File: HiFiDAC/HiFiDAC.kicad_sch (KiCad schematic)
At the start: 48 parts, among them J1 SE, J2 I2S, J3 LDIFF, J4 RDIFF, J5 CTRL, J6 5V, J7 +-15V, U1 PCM1794A

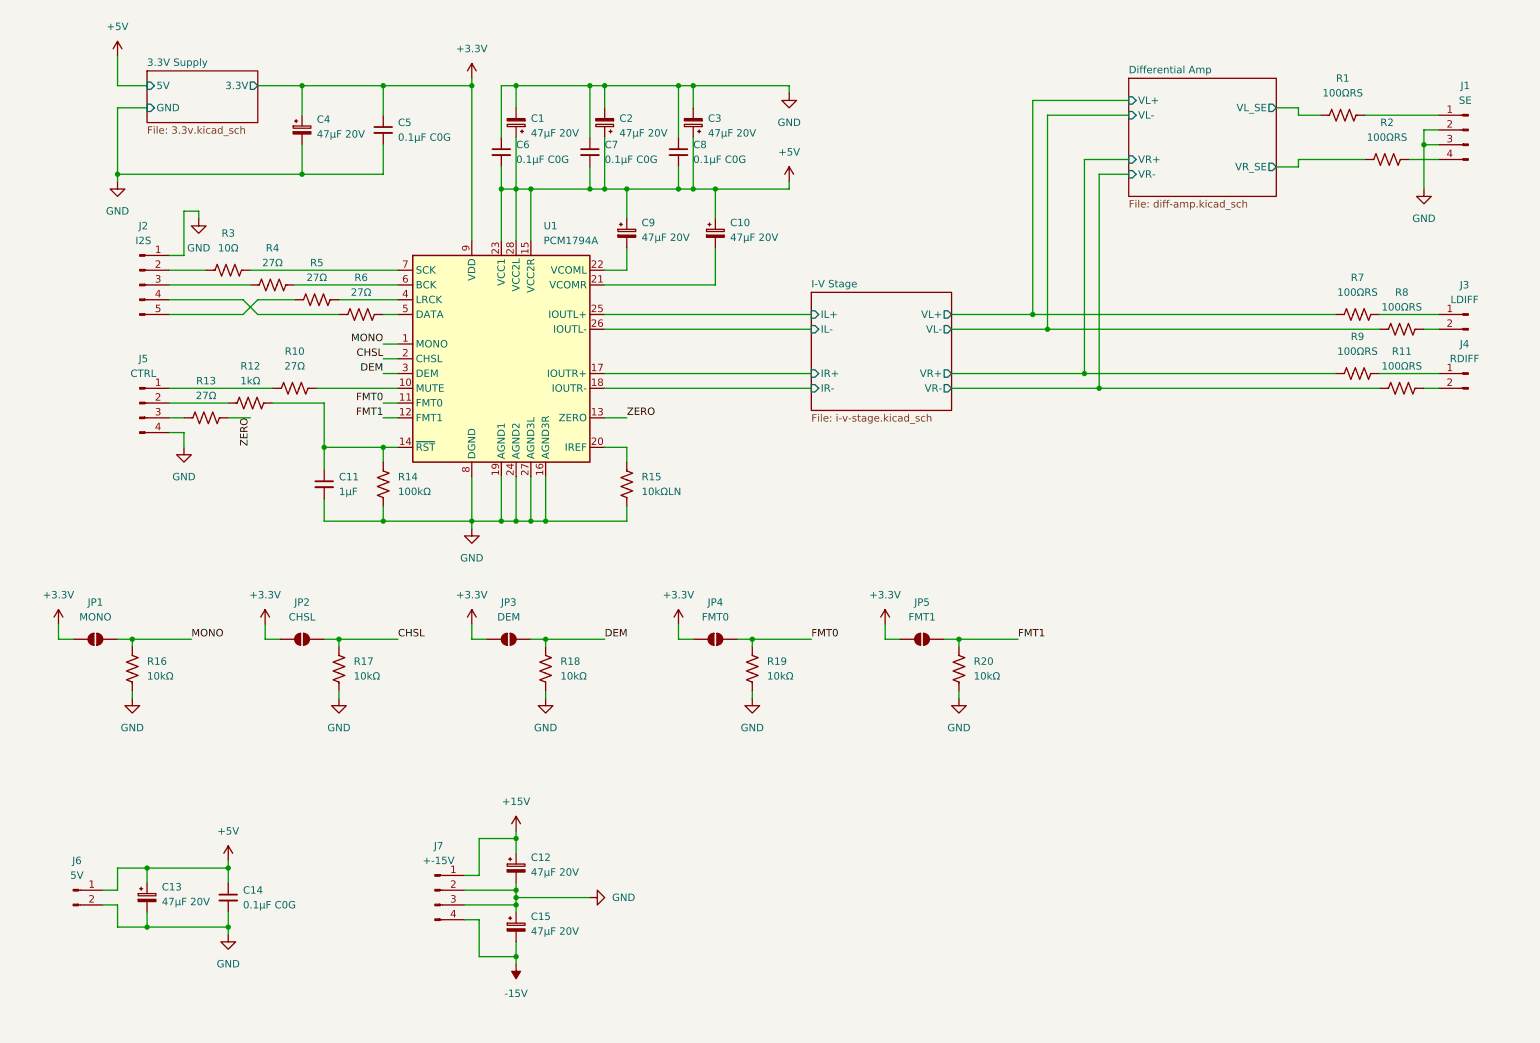
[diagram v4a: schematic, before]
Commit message: HiFiDAC redesign of clocking, digital IO, ferrite beads
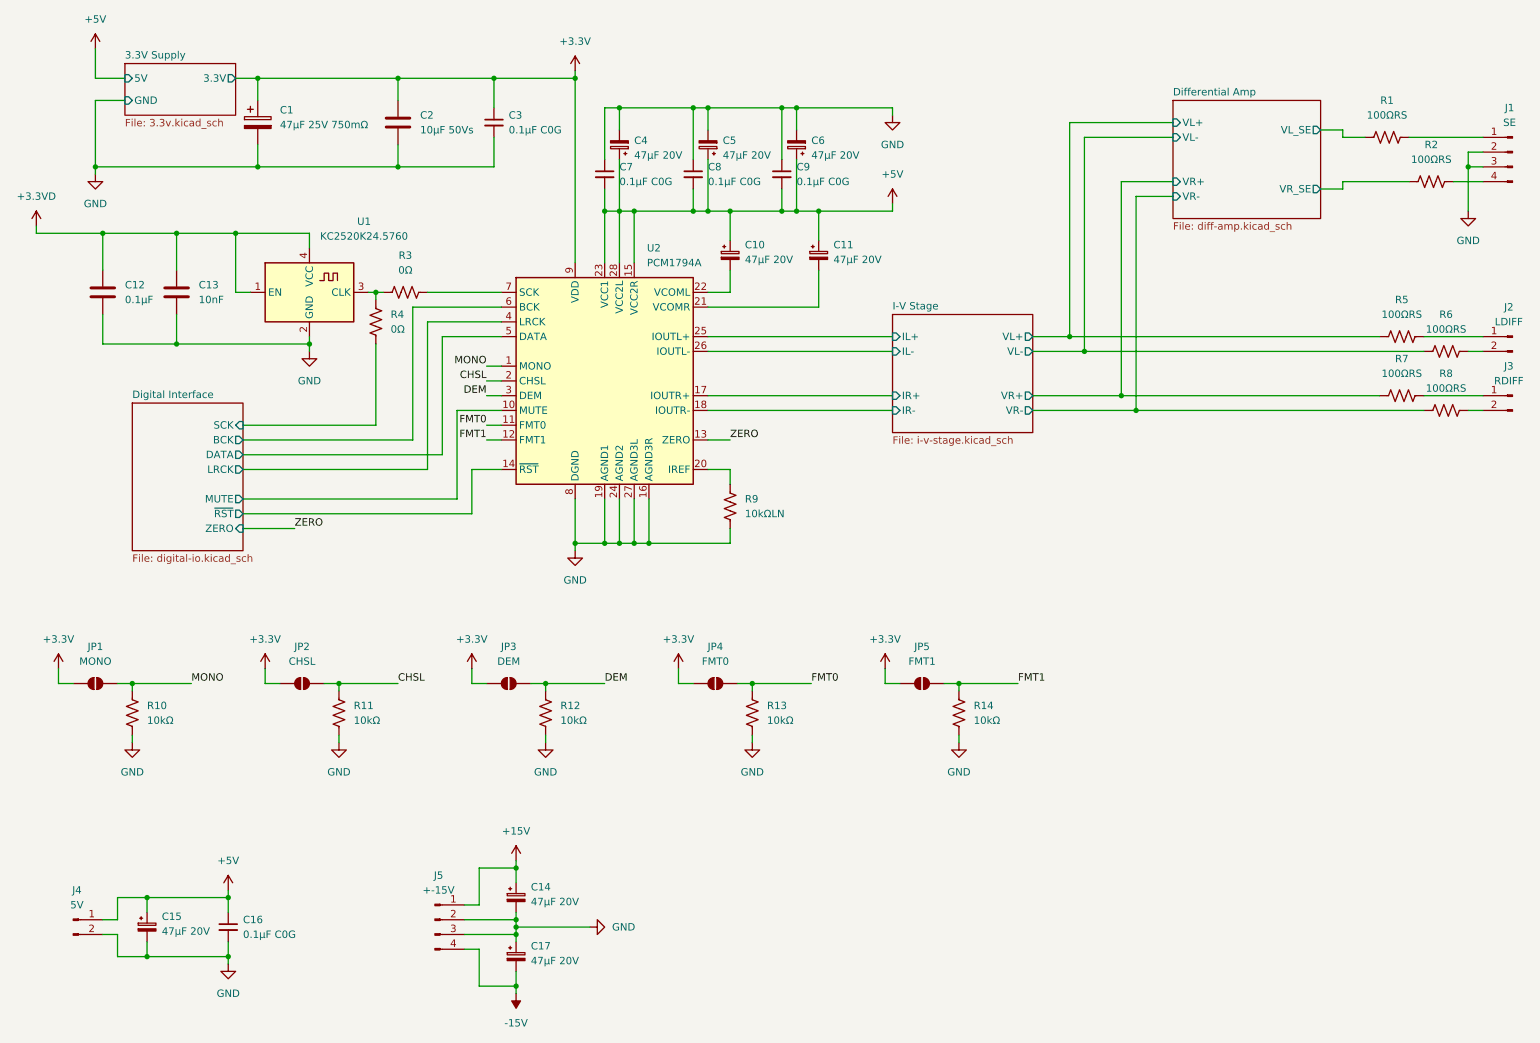
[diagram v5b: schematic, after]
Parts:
- removed C11: 1µF, Capacitor_SMD:C_0603_1608Metric, symbol Device:C_Small
- removed J2: I2S, BW_Connectors:Amphenol_MINITEK_0.8_5P_V, symbol Connector:Conn_01x05_Pin
- removed J5: CTRL, BW_Connectors:Amphenol_MINITEK_0.8_4P_V, symbol Connector:Conn_01x04_Pin
- removed R10, R13, R5, R6: 27Ω, Resistor_SMD:R_0603_1608Metric, symbol Device:R_US
- removed R12: 1kΩ, Resistor_SMD:R_0603_1608Metric, symbol Device:R_US
- removed R14: 100kΩ, Resistor_SMD:R_0603_1608Metric, symbol Device:R_US
- added C12: 0.1µF, Capacitor_SMD:C_0603_1608Metric, symbol Device:C
- added C13: 10nF, Capacitor_SMD:C_0603_1608Metric, symbol Device:C
- added C2: 10µF 50Vs, Capacitor_SMD:C_0805_2012Metric, symbol Device:C
- added U1: KC2520K24.5760, Oscillator:Oscillator_SMD_Kyocera_KC2520Z-4Pin_2.5x2.0mm, symbol BW_Active:KC2520K
- C1: renamed from C4; value 47µF 20V -> 47µF 25V 750mΩ; footprint Capacitor_SMD:CP_Elec_5x5.8 -> Capacitor_SMD:CP_Elec_6.3x7.7; symbol Device:C_Polarized_Small -> Device:C_Polarized
- R3: value 10Ω -> 0Ω
- R4: value 27Ω -> 0Ω
- renumbered C9 to C10, C10 to C11, C12 to C14, C13 to C15, C14 to C16, C15 to C17, C5 to C3, C1 to C4, C2 to C5, C3 to C6, C6 to C7, C7 to C8, C8 to C9, J3 to J2, J4 to J3, J6 to J4, J7 to J5, R16 to R10, R17 to R11, R18 to R12, R19 to R13, R20 to R14, R7 to R5, R8 to R6, R9 to R7, R11 to R8, R15 to R9, U1 to U2
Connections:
- net +3.3V: now also C2.1
- net GND: now also C12.2, C13.2, C2.2, U1.2 (GND)
- net Digital Interface/LRCK: now reaches U2.4 (LRCK)
- net at R3.1: now also R4.2, U1.3 (CLK)
- net Digital Interface/SCK: now reaches R4.1
- net Digital Interface/DATA: now reaches U2.5 (DATA)
- net Digital Interface/~{RST}: now reaches U2.14 (~{RST})
- net Digital Interface/MUTE: now reaches U2.10 (MUTE)
- net Digital Interface/BCK: now reaches U2.6 (BCK)
- net Digital Interface/BCK: no longer R4.2
- new net +3.3VD: C12.1, C13.1, U1.1 (EN), U1.4 (VCC)
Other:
- added sheet Digital Interface (digital-io.kicad_sch)
- moved on the sheet: C1, C10, C11, C14, C15, C16, C17, C3, C4, C5, C6, C7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

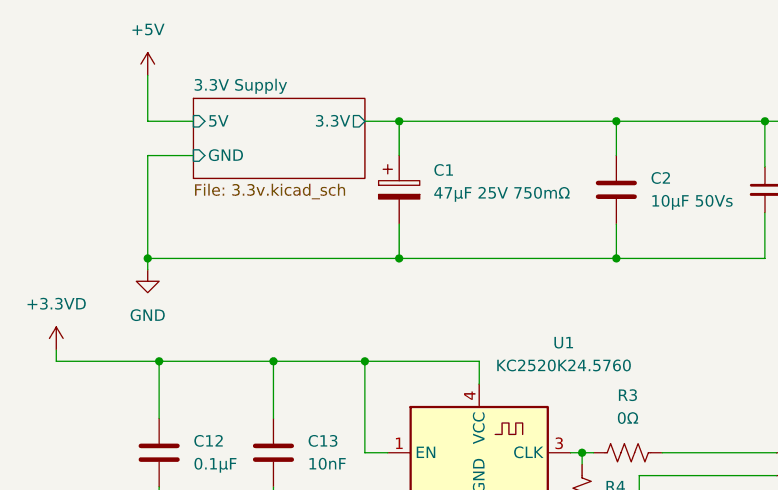
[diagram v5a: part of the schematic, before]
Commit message: HiFiDAC initial layout complete
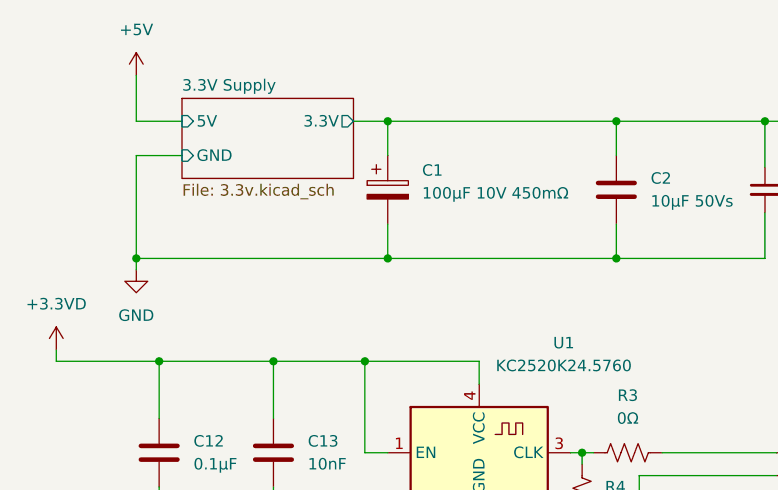
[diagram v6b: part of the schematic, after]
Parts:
- C1: value 47µF 25V 750mΩ -> 100µF 10V 450mΩ
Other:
- moved on the sheet: C1
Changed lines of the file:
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@@
 	)
 	(junction
-		(at 35.56 43.18)
+		(at 34.29 43.18)
 		(diameter 0)
 		(color 0 0 0 0)
@@
 	)
 	(junction
-		(at 63.5 43.18)
+		(at 62.23 43.18)
 		(diameter 0)
 		(color 0 0 0 0)
@@
 	)
 	(junction
-		(at 63.5 27.94)
+		(at 62.23 27.94)
 		(diameter 0)
 		(color 0 0 0 0)
@@
 	(wire
 		(pts
-			(xy 59.69 27.94) (xy 63.5 27.94)
+			(xy 58.42 27.94) (xy 62.23 27.94)
 		)
 		(stroke
@@
 	(wire
 		(pts
-			(xy 35.56 27.94) (xy 40.64 27.94)
+			(xy 34.29 27.94) (xy 39.37 27.94)
 		)
 		(stroke
@@
 	(wire
 		(pts
-			(xy 35.56 31.75) (xy 40.64 31.75)
+			(xy 34.29 31.75) (xy 39.37 31.75)
 		)
 		(stroke
@@
 	(wire
 		(pts
-			(xy 63.5 39.37) (xy 63.5 43.18)
+			(xy 62.23 39.37) (xy 62.23 43.18)
 		)
 		(stroke
@@
 	(wire
 		(pts
-			(xy 35.56 43.18) (xy 35.56 31.75)
+			(xy 34.29 43.18) (xy 34.29 31.75)
 		)
 		(stroke
@@
 	(wire
 		(pts
-			(xy 35.56 22.86) (xy 35.56 27.94)
+			(xy 34.29 22.86) (xy 34.29 27.94)
 		)
 		(stroke
@@
 	(wire
 		(pts
-			(xy 35.56 43.18) (xy 63.5 43.18)
+			(xy 34.29 43.18) (xy 62.23 43.18)
 		)
 		(stroke
@@
 	(wire
 		(pts
-			(xy 35.56 44.45) (xy 35.56 43.18)
+			(xy 34.29 44.45) (xy 34.29 43.18)
 		)
 		(stroke
@@
 	(wire
 		(pts
-			(xy 63.5 43.18) (xy 87.63 43.18)
+			(xy 62.23 43.18) (xy 87.63 43.18)
 		)
 		(stroke
@@
 	(wire
 		(pts
-			(xy 63.5 27.94) (xy 87.63 27.94)
+			(xy 62.23 27.94) (xy 87.63 27.94)
 		)
 		(stroke
@@
 	(wire
 		(pts
-			(xy 63.5 27.94) (xy 63.5 31.75)
+			(xy 62.23 27.94) (xy 62.23 31.75)
 		)
 		(stroke
@@
 	(symbol
 		(lib_id "power:GND")
-		(at 35.56 44.45 0)
+		(at 34.29 44.45 0)
 		(unit 1)
 		(exclude_from_sim no)
@@
 		(fields_autoplaced yes)
 		(property "Reference" "#PWR04"
-			(at 35.56 50.8 0)
+			(at 34.29 50.8 0)
 			(effects
 				(font
@@
 		)
 		(property "Value" "GND"
-			(at 35.56 49.53 0)
+			(at 34.29 49.53 0)
 			(effects
 				(font
@@
 		)
 		(property "Footprint" ""
-			(at 35.56 44.45 0)
+			(at 34.29 44.45 0)
 			(effects
 				(font
@@
 		)
 		(property "Datasheet" ""
-			(at 35.56 44.45 0)
+			(at 34.29 44.45 0)
 			(effects
 				(font
@@
 		)
 		(property "Description" "Power symbol creates a global label with name \"GND\" , ground"
-			(at 35.56 44.45 0)
+			(at 34.29 44.45 0)
 			(effects
 				(font
@@
 	(symbol
 		(lib_id "Device:C_Polarized")
-		(at 63.5 35.56 0)
+		(at 62.23 35.56 0)
 		(unit 1)
 		(exclude_from_sim no)
@@
 		(fields_autoplaced yes)
 		(property "Reference" "C1"
-			(at 67.31 33.4009 0)
+			(at 66.04 33.4009 0)
 			(effects
 				(font
@@
 			)
 		)
-		(property "Value" "47µF 25V 750mΩ"
-			(at 67.31 35.9409 0)
+		(property "Value" "100µF 10V 450mΩ"
+			(at 66.04 35.9409 0)
 			(effects
 				(font
@@
 		)
 		(property "Footprint" "Capacitor_SMD:CP_Elec_6.3x7.7"
-			(at 64.4652 39.37 0)
+			(at 63.1952 39.37 0)
 			(effects
 				(font
@@
 		)
 		(property "Datasheet" "~"
-			(at 63.5 35.56 0)
+			(at 62.23 35.56 0)
 			(effects
 				(font
@@
 		)
 		(property "Description" "Polarized capacitor"
-			(at 63.5 35.56 0)
+			(at 62.23 35.56 0)
 			(effects
 				(font
@@
 	(symbol
 		(lib_id "power:+5V")
-		(at 35.56 22.86 0)
+		(at 34.29 22.86 0)
 		(unit 1)
 		(exclude_from_sim no)
@@
 		(fields_autoplaced yes)
 		(property "Reference" "#PWR01"
-			(at 35.56 26.67 0)
+			(at 34.29 26.67 0)
 			(effects
 				(font
@@
 		)
 		(property "Value" "+5V"
-			(at 35.56 17.78 0)
+			(at 34.29 17.78 0)
 			(effects
 				(font
@@
 		)
 		(property "Footprint" ""
-			(at 35.56 22.86 0)
+			(at 34.29 22.86 0)
 			(effects
 				(font
@@
 		)
 		(property "Datasheet" ""
-			(at 35.56 22.86 0)
+			(at 34.29 22.86 0)
 			(effects
 				(font
@@
 		)
 		(property "Description" "Power symbol creates a global label with name \"+5V\""
-			(at 35.56 22.86 0)
+			(at 34.29 22.86 0)
 			(effects
 				(font
@@
 	)
 	(sheet
-		(at 40.64 25.4)
+		(at 39.37 25.4)
 		(size 19.05 8.89)
 		(fields_autoplaced yes)
@@
 		)
 		(property "Sheetname" "3.3V Supply"
-			(at 40.64 24.6884 0)
+			(at 39.37 24.6884 0)
 			(effects
 				(font
@@
 		)
 		(property "Sheetfile" "3.3v.kicad_sch"
-			(at 40.64 34.8746 0)
+			(at 39.37 34.8746 0)
 			(effects
 				(font
@@
 		)
 		(pin "5V" input
-			(at 40.64 27.94 180)
+			(at 39.37 27.94 180)
 			(effects
 				(font
@@
 		)
 		(pin "GND" input
-			(at 40.64 31.75 180)
+			(at 39.37 31.75 180)
 			(effects
 				(font
@@
 		)
 		(pin "3.3V" output
-			(at 59.69 27.94 0)
+			(at 58.42 27.94 0)
 			(effects
 				(font

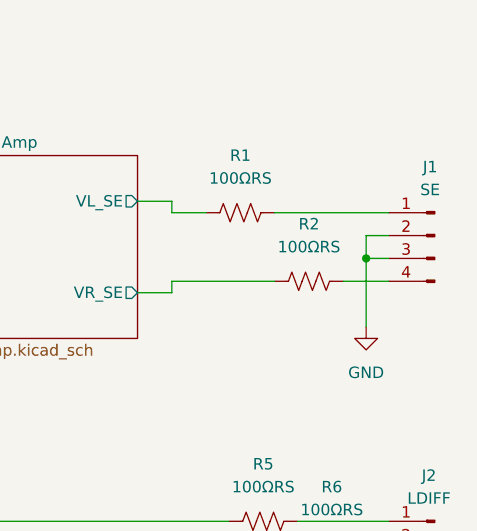
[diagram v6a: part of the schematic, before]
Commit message: HiFiDAC routing initially complete
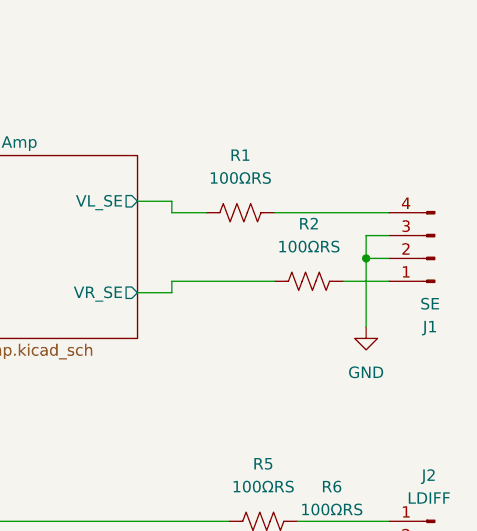
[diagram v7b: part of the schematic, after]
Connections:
- net at J1.1 (Pin_1): now also R2.1; no longer R1.1
- net at J1.4 (Pin_4): now also R1.1; no longer R2.1
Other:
- moved on the sheet: J1
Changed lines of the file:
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@@
 	)
 	(junction
-		(at 271.78 43.18)
-		(diameter 0)
-		(color 0 0 0 0)
-	)
-	(junction
 		(at 138.43 33.02)
 		(diameter 0)
@@
 	)
 	(junction
+		(at 271.78 43.18)
+		(diameter 0)
+		(color 0 0 0 0)
+	)
+	(junction
 		(at 44.45 179.07)
 		(diameter 0)
@@
 	(wire
 		(pts
+			(xy 271.78 43.18) (xy 271.78 50.8)
+		)
+		(stroke
+			(width 0)
+			(type default)
+		)
+	)
+	(wire
+		(pts
 			(xy 92.71 69.85) (xy 92.71 95.25)
 		)
@@
 	(wire
 		(pts
-			(xy 271.78 43.18) (xy 271.78 50.8)
-		)
-		(stroke
-			(width 0)
-			(type default)
-		)
-	)
-	(wire
-		(pts
 			(xy 92.71 64.77) (xy 105.41 64.77)
 		)
@@
 	(wire
 		(pts
-			(xy 274.32 40.64) (xy 271.78 40.64)
+			(xy 58.42 167.64) (xy 58.42 168.91)
 		)
 		(stroke
@@
 	(wire
 		(pts
-			(xy 58.42 167.64) (xy 58.42 168.91)
+			(xy 105.41 72.39) (xy 95.25 72.39)
 		)
 		(stroke
@@
 	(wire
 		(pts
-			(xy 105.41 72.39) (xy 95.25 72.39)
+			(xy 138.43 46.99) (xy 138.43 50.8)
 		)
 		(stroke
@@
 	(wire
 		(pts
-			(xy 138.43 46.99) (xy 138.43 50.8)
+			(xy 261.62 38.1) (xy 274.32 38.1)
 		)
 		(stroke
@@
 	(wire
 		(pts
+			(xy 271.78 40.64) (xy 274.32 40.64)
+		)
+		(stroke
+			(width 0)
+			(type default)
+		)
+	)
+	(wire
+		(pts
 			(xy 125.73 50.8) (xy 123.19 50.8)
 		)
@@
 	(wire
 		(pts
-			(xy 271.78 43.18) (xy 274.32 43.18)
-		)
-		(stroke
-			(width 0)
-			(type default)
-		)
-	)
-	(wire
-		(pts
 			(xy 90.17 90.17) (xy 60.96 90.17)
 		)
@@
 	(wire
 		(pts
+			(xy 271.78 43.18) (xy 274.32 43.18)
+		)
+		(stroke
+			(width 0)
+			(type default)
+		)
+	)
+	(wire
+		(pts
 			(xy 100.33 102.87) (xy 60.96 102.87)
 		)
@@
 	(wire
 		(pts
-			(xy 261.62 38.1) (xy 274.32 38.1)
-		)
-		(stroke
-			(width 0)
-			(type default)
-		)
-	)
-	(wire
-		(pts
 			(xy 135.89 129.54) (xy 135.89 132.08)
 		)
@@
 	(symbol
 		(lib_id "Connector:Conn_01x04_Pin")
-		(at 279.4 40.64 0)
-		(mirror y)
+		(at 279.4 43.18 180)
 		(unit 1)
 		(exclude_from_sim no)
@@
 		(dnp no)
 		(property "Reference" "J1"
-			(at 278.892 33.02 0)
+			(at 278.892 50.8 0)
 			(effects
 				(font
@@
 		)
 		(property "Value" "SE"
-			(at 278.892 35.56 0)
+			(at 278.892 48.26 0)
 			(effects
 				(font
@@
 		)
 		(property "Footprint" "BW_Connectors:Amphenol_MINITEK_0.8_4P_V"
-			(at 279.4 40.64 0)
+			(at 279.4 43.18 0)
 			(effects
 				(font
@@
 		)
 		(property "Datasheet" "~"
-			(at 279.4 40.64 0)
+			(at 279.4 43.18 0)
 			(effects
 				(font
@@
 		)
 		(property "Description" "Generic connector, single row, 01x04, script generated"
-			(at 279.4 40.64 0)
+			(at 279.4 43.18 0)
 			(effects
 				(font

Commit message: HiFiDAC v2 progress
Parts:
- removed C1: 100µF 10V 450mΩ, Capacitor_SMD:CP_Elec_6.3x7.7, symbol Device:C_Polarized
- removed C10, C11, C15, C4, C5, C6: 47µF 20V, Capacitor_SMD:CP_Elec_5x5.8, symbol Device:C_Polarized_Small
- removed C7, C8, C9: 0.1µF C0G, BW_PassiveMechanical:C_0704_1810Metric, symbol Device:C_Small
- removed JP1: MONO, Jumper:SolderJumper-2_P1.3mm_Open_RoundedPad1.0x1.5mm, symbol Jumper:SolderJumper_2_Open
- removed JP2: CHSL, Jumper:SolderJumper-2_P1.3mm_Open_RoundedPad1.0x1.5mm, symbol Jumper:SolderJumper_2_Open
- removed JP3: DEM, Jumper:SolderJumper-2_P1.3mm_Open_RoundedPad1.0x1.5mm, symbol Jumper:SolderJumper_2_Open
- removed JP4: FMT0, Jumper:SolderJumper-2_P1.3mm_Open_RoundedPad1.0x1.5mm, symbol Jumper:SolderJumper_2_Open
- removed JP5: FMT1, Jumper:SolderJumper-2_P1.3mm_Open_RoundedPad1.0x1.5mm, symbol Jumper:SolderJumper_2_Open
- removed R1, R2, R5, R6, R7, R8: 100ΩRS, Resistor_SMD:R_0805_2012Metric, symbol Device:R_US
- removed R10, R11, R12, R13, R14: 10kΩ, Resistor_SMD:R_0603_1608Metric, symbol Device:R_US
- removed R9: 10kΩLN, Resistor_SMD:R_0603_1608Metric, symbol Device:R_US
- removed U2: PCM1794A, Package_SO:SSOP-28_5.3x10.2mm_P0.65mm, symbol Audio:PCM1794A
- added C4: 100µF 10V 450mΩ, Capacitor_SMD:CP_Elec_6.3x7.7, symbol Device:C_Polarized
- C2: value 10µF 50Vs -> 1µF 25V; footprint Capacitor_SMD:C_0805_2012Metric -> Capacitor_SMD:C_0603_1608Metric
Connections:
- net +5V: now also C4.1
- net GND: now also C4.2
- net I-V Stage/VL+: now reaches J2.1 (Pin_1)
- net I-V Stage/VL+: now also J1.4 (Pin_4)
- net I-V Stage/VL-: now reaches J2.2 (Pin_2)
- net I-V Stage/VR+: now reaches J3.1 (Pin_1)
- net I-V Stage/VR+: now also J1.1 (Pin_1)
- net I-V Stage/VR-: now reaches J3.2 (Pin_2)
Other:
- removed sheet Differential Amp
- moved on the sheet: C16, J4
